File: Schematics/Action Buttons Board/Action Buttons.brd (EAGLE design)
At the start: 54.3 x 67.3 mm, 11 parts

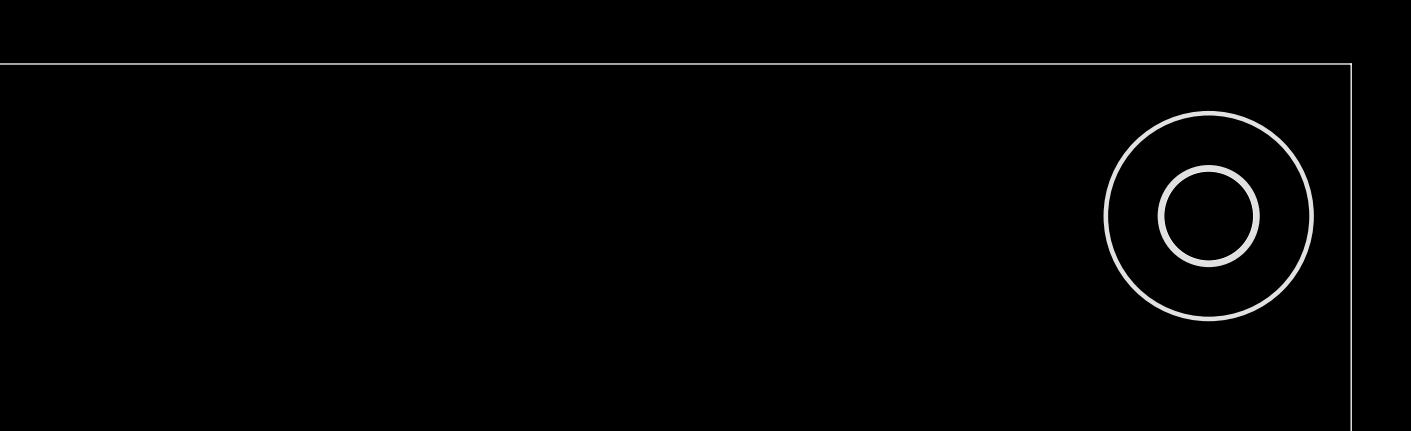
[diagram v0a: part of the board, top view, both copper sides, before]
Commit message: Schematics updated External Controller board schematic created
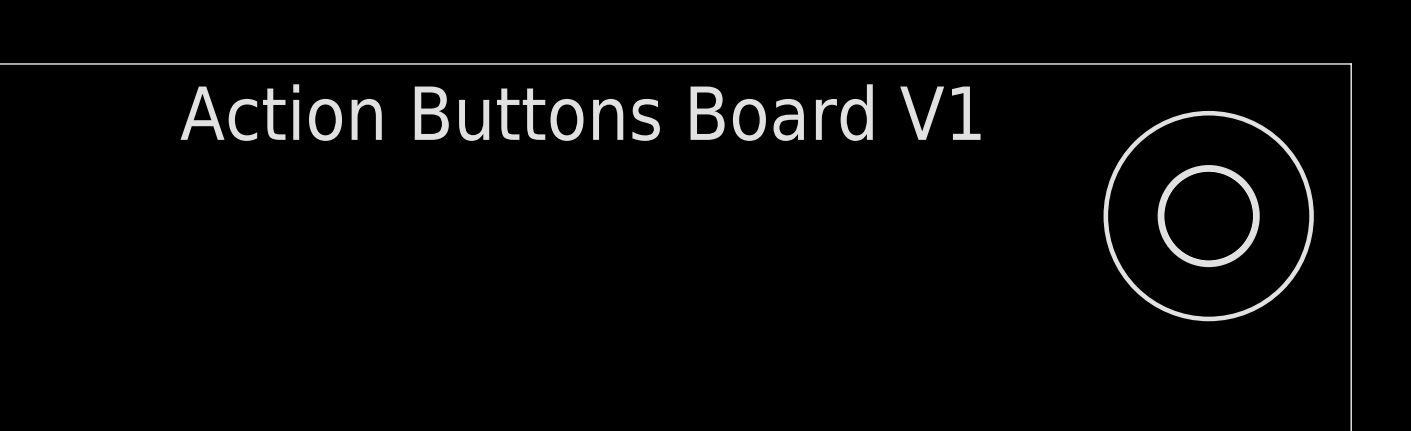
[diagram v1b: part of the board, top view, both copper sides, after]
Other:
- board text added: "Action Buttons Board V1"
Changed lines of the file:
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@@
 <wire x1="54.28" y1="67.3" x2="0" y2="67.3" width="0" layer="20"/>
 <wire x1="0" y1="67.3" x2="0" y2="0" width="0" layer="20"/>
+<text x="15.24" y="64.77" size="1.778" layer="25">Action Buttons Board V1</text>
 </plain>
 <attributes>
